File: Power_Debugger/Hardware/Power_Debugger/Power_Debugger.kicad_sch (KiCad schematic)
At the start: 30 parts, among them J1 632722100213, J2 Screw_Terminal_01x02, Q1 FS8205A, Q2 FS8205A, U1 BQ24092DGQT, U2 DW01A, U3 TPS611781RNWR

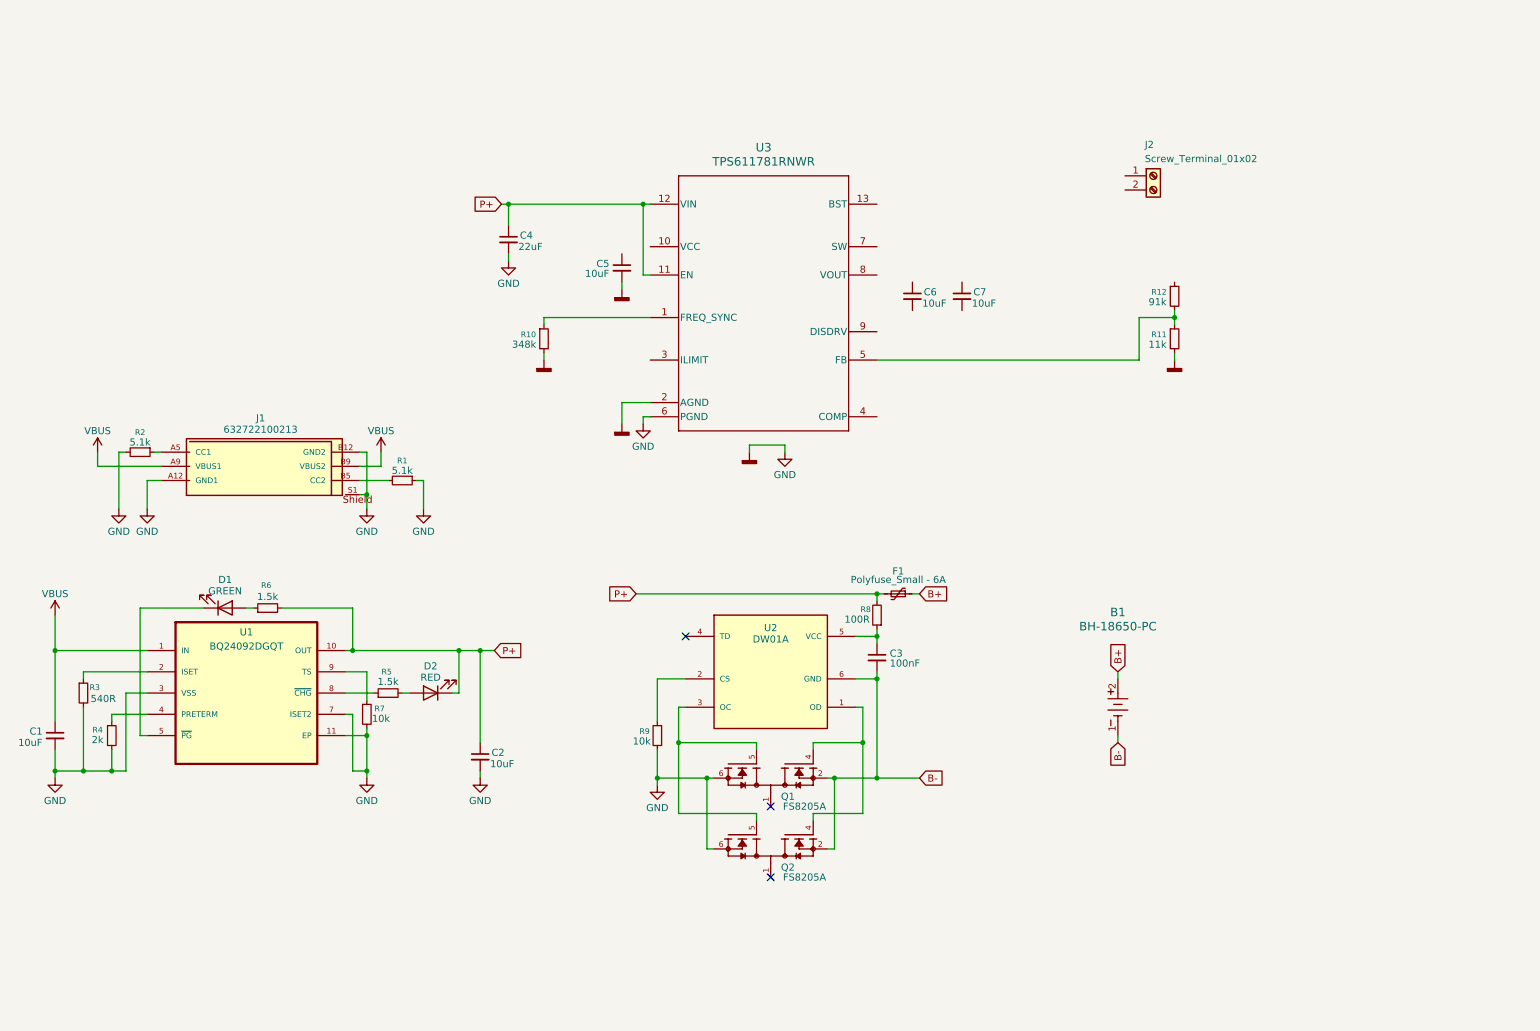
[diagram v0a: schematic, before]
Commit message: feat(Power Debugger): complete Boost + fix
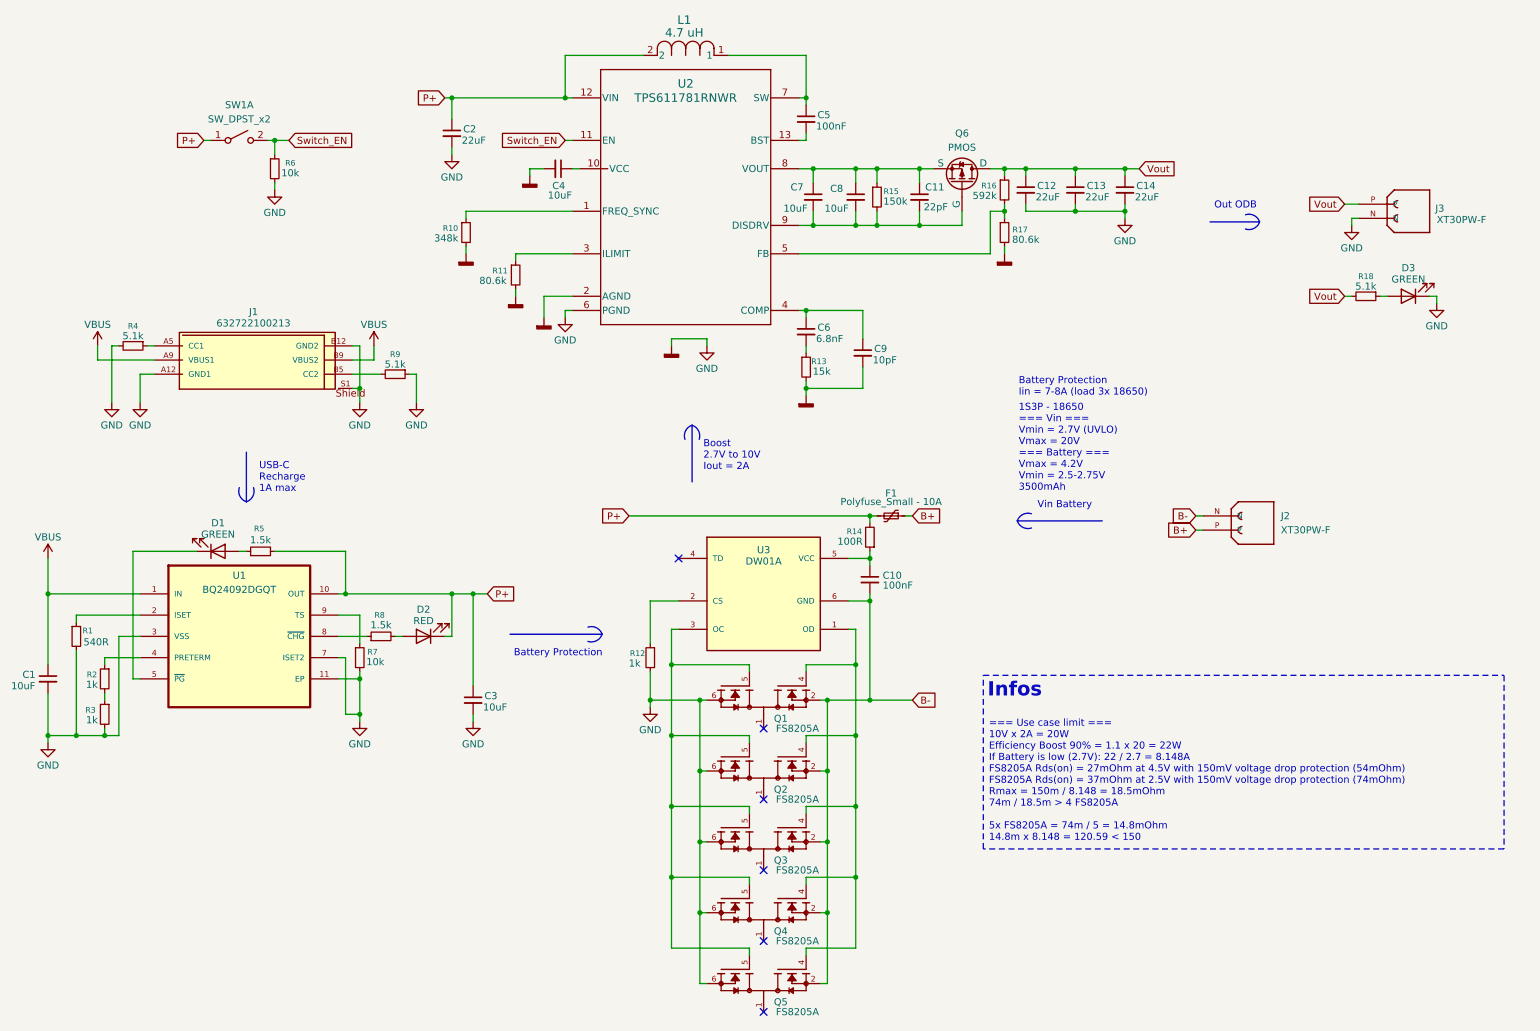
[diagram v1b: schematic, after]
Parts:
- removed B1: BH-18650-PC, BAT_BH-18650-PC_MPD, symbol Power_Debugger_Library:BH-18650-PC
- removed J2: Screw_Terminal_01x02, symbol Connector:Screw_Terminal_01x02
- removed R4: 2k, symbol Device:R_Small
- added C11: 22pF, symbol Device:C_Small
- added C12, C13, C14: 22uF, symbol Device:C_Small
- added C5: 100nF, symbol Device:C_Small
- added C8: 10uF, symbol Device:C_Small
- added C9: 10pF, symbol Device:C_Small
- added D3: GREEN, symbol Device:LED
- added J2, J3: XT30PW-F, XT30PW-F:AMASS_XT30PW-F, symbol Power_Debugger_Library:XT30PW-F
- added L1: 4.7 uH, ODB:IND_PA4342_PUL, symbol ODB2:PA4342.472NLT
- added Q3, Q4, Q5: FS8205A, FS8205A:SOP65P640X120-8N, symbol Power_Debugger_Library:FS8205A
- added Q6: PMOS, symbol Simulation_SPICE:PMOS
- added R11: 80.6k, symbol Device:R_Small
- added R13: 15k, symbol Device:R_Small
- added R15: 150k, symbol Device:R_Small
- added R18: 5.1k, symbol Device:R_Small
- added R2, R3: 1k, symbol Device:R_Small
- added R6: 10k, symbol Device:R_Small
- added SW1: SW_DPST_x2, symbol Switch:SW_DPST_x2
- C6: value 10uF -> 6.8nF
- F1: value Polyfuse_Small - 6A -> Polyfuse_Small - 10A
- R12: renamed from R9; value 10k -> 1k
- R16: renamed from R12; value 91k -> 592k
- R17: renamed from R11; value 11k -> 80.6k
- renumbered C3 to C10, C4 to C2, C2 to C3, C5 to C4, R3 to R1, R8 to R14, R2 to R4, R6 to R5, R5 to R8, R1 to R9, U3 to U2, U2 to U3
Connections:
- net B+: now also J2.P
- net B-: now also J2.N, Q3.2, Q3.3, Q4.2, Q4.3, Q5.2, Q5.3
- net P+: now also L1.2, SW1.1 (A); no longer U2.11 (EN)
- net at U2.10 (VCC): now also C4.1
- net at U2.13 (BST): now also C5.2
- net at U2.3 (ILIMIT): now also R11.1
- net at U2.4 (COMP): now also C6.1, C9.1
- net at U2.7 (SW): now also C5.1, L1.1
- net at U2.8 (VOUT): now also C7.1, C11.1, C8.1, Q6.3 (S), R15.1
- net at U2.9 (DISDRV): now also C7.2, C11.2, C8.2, Q6.2 (G), R15.2
- net at Q1.4, Q2.4, U3.1 (OD): now also Q3.4, Q4.4, Q5.4
- net at Q1.5, Q2.5, U3.3 (OC): now also Q3.5, Q4.5, Q5.5
- net at C6.2: now also R13.1
- net at U1.4 (PRETERM): now also R2.1
- net Vout: now reaches R16.1
- net Vout: now also C12.1, C13.1, C14.1, J3.P, Q6.1 (D), R18.2
- net GND renamed AGND5V
- net AGND5V: now also C12.2, C13.2, C14.2, C9.2, D3.1 (K), J3.N, Q3.6, Q3.7, Q4.6, Q4.7, Q5.6, Q5.7, R11.2, R13.2, R3.2, R6.2
- new net: R2.2, R3.1
- new net: Q3.1, Q3.8
- new net: D3.2 (A), R18.1
- new net: Q5.1, Q5.8
- new net: Q4.1, Q4.8
- new net Switch_EN: R6.1, SW1.2 (B), U2.11 (EN)
- no-connect marks 3 -> 6
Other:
- note added: "1S3P - 18650 === Vin === Vmin = 2.7V (UVLO) Vmax = 20V === Battery === Vmax = 4.2V Vmin = 2.5-2.75V 3500mAh"
- note added: "=== Use case limit === 10V x 2A = 20W Efficiency Boost 90% = 1.1 x 20 = 22W If Battery is low (2.7V): 22 / 2.7 = 8.148A FS8205A Rds(on) = 27mOhm at 4.5V with 150mV voltage drop protection (54mOhm) FS8205A Rds(on) = 37mOhm at 2.5V with 150mV voltage drop protection (74mOhm) Rmax = 150m / 8.148 = 18.5mOhm 74m / 18.5m > 4 FS8205A 5x FS8205A = 74m / 5 = 14.8mOhm 14.8m x 8.148 = 120.59 < 150"
- note added: "Battery Protection"
- note added: "Battery Protection Iin = 7-8A (load 3x 18650)"
- note added: "Boost 2.7V to 10V Iout = 2A"
- note added: "Infos"
- note added: "Out ODB"
- note added: "USB-C Recharge 1A max"
- note added: "Vin Battery"
- moved on the sheet: C1, C10, C2, C3, C4, D1, D2, F1, J1, Q1, Q2, R1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
